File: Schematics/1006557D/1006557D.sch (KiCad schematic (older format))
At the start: 9 parts, among them J1 ConnectorBlockI, X1 OvalBody2, X2 NorBody, X3 ArrowTwiddle, X4 ArrowTwiddle

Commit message: Completed and proofed CAD transcription of drawing 1006557D (Block I AGC module A36 electrical schematic).
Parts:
- added unit 73 of J1
- added unit 70 of J1
- added unit 77 of J1
- added unit 76 of J1
- added unit 75 of J1
- added unit 79 of J1
- added unit 129 of J1
- added unit 74 of J1
- added unit 128 of J1
- added unit 49 of J1
- added unit 45 of J1
- added unit 43 of J1
- added unit 41 of J1
- added unit 62 of J1
- added unit 65 of J1
- added unit 111 of J1
- added unit 113 of J1
- added unit 114 of J1
- added unit 115 of J1
- added unit 116 of J1
- added unit 117 of J1
- added unit 118 of J1
- added unit 50 of J1
- added unit 53 of J1
- added unit 52 of J1
- added unit 54 of J1
- added unit 57 of J1
- added unit 56 of J1
- added unit 36 of J1
- added unit 64 of J1
- added unit 103 of J1
- added unit 101 of J1
- added unit 100 of J1
- added unit 107 of J1
- added unit 106 of J1
- added unit 105 of J1
- added unit 109 of J1
- added unit 108 of J1
- added unit 28 of J1
- added unit 29 of J1
- added unit 25 of J1
- added unit 27 of J1
- added unit 21 of J1
- added unit 16 of J1
- added unit 14 of J1
- added unit 58 of J1
- added unit 137 of J1
- added unit 135 of J1
- added unit 130 of J1
- added unit 131 of J1
- added unit 39 of J1
- added unit 38 of J1
- added unit 102 of J1
- added unit 33 of J1
- added unit 32 of J1
- added unit 20 of J1
- added unit 12 of J1
- added unit 124 of J1
- added unit 122 of J1
- added unit 125 of J1
- added unit 127 of J1
- added unit 126 of J1
- added unit 9 of J1
- added unit 2 of J1
- added unit 90 of J1
- added unit 1 of J1
- added unit 4 of J1
- added unit 139 of J1
- added unit 83 of J1
- added unit 80 of J1
- added unit 81 of J1
- added unit 86 of J1
- added unit 87 of J1
- added unit 84 of J1
- added unit 85 of J1
- added unit 89 of J1
- added unit 15 of J1
- added unit 11 of J1
- added unit 19 of J1
- added unit 18 of J1
- added unit 99 of J1
- added unit 98 of J1
- added unit 94 of J1
- added unit 97 of J1
- added unit 91 of J1
- added unit 82 of J1
- added unit 92 of J1
- added unit 46 of J1
- added unit 63 of J1
- added unit 67 of J1
- added unit 68 of J1
- added unit 69 of J1
- added unit 104 of J1
- added unit 40 of J1
- added unit 142 of J1
- added unit 141 of J1
- added unit 140 of J1
- added unit 42 of J1
- added unit 110 of J1
- added U1, U10, U12, U73, U80, U81, U9: D3NOR-+3VDC-0VDC-block1-1_3-___, symbol D3NOR-+3VDC-0VDC-block1:D3NOR-+3VDC-0VDC-block1-1_3-___
- added U100, U104, U108, U120, U5, U72, U92: D3NOR-+3VDC-0VDC-block1-3_5-___, symbol D3NOR-+3VDC-0VDC-block1:D3NOR-+3VDC-0VDC-block1-3_5-___
- added U101, U107, U119, U13, U18, U21, U22, U26, U37, U41, U42, U45, U46, U52, U53, U57, U69, U70, U78, U82: D3NOR-+3VDC-0VDC-block1-_3_-___, symbol D3NOR-+3VDC-0VDC-block1:D3NOR-+3VDC-0VDC-block1-_3_-___
- added U102, U11, U110, U118, U85, U89, U97: D3NOR-+3VDC-0VDC-block1-13_-___, symbol D3NOR-+3VDC-0VDC-block1:D3NOR-+3VDC-0VDC-block1-13_-___
- added U106, U16, U20, U55, U71, U75, U87, U91, U95, U99: D3NOR-+3VDC-0VDC-block1-153-___, symbol D3NOR-+3VDC-0VDC-block1:D3NOR-+3VDC-0VDC-block1-153-___
- added U109, U113, U117, U17, U29, U30, U38, U50, U54, U61, U62, U90, U93, U94, U98: D3NOR-+3VDC-0VDC-block1-_1_-___, symbol D3NOR-+3VDC-0VDC-block1:D3NOR-+3VDC-0VDC-block1-_1_-___
- added U111, U115, U64: D3NOR-NC-0VDC-expander-block1-_5_-___, symbol D3NOR-NC-0VDC-expander-block1:D3NOR-NC-0VDC-expander-block1-_5_-___
- added U114, U8: D3NOR-+3VDC-0VDC-block1-31_-___, symbol D3NOR-+3VDC-0VDC-block1:D3NOR-+3VDC-0VDC-block1-31_-___
- added U14: D3NOR-NC-0VDC-expander-block1-1_3-___, symbol D3NOR-NC-0VDC-expander-block1:D3NOR-NC-0VDC-expander-block1-1_3-___
- added U15, U19, U23, U27, U28, U3, U31, U35, U39, U47, U51, U59, U63, U7, U79, U83: D3NOR-+3VDC-0VDC-block1-135-___, symbol D3NOR-+3VDC-0VDC-block1:D3NOR-+3VDC-0VDC-block1-135-___
- added U24, U32, U36, U4, U40, U43, U44, U48, U84, U88, U96: D3NOR-+3VDC-0VDC-block1-315-___, symbol D3NOR-+3VDC-0VDC-block1:D3NOR-+3VDC-0VDC-block1-315-___
- added U25, U33, U34, U65, U67, U86: D3NOR-+3VDC-0VDC-block1-_5_-___, symbol D3NOR-+3VDC-0VDC-block1:D3NOR-+3VDC-0VDC-block1-_5_-___
- added U6, U60, U68, U76: D3NOR-+3VDC-0VDC-block1-1_5-___, symbol D3NOR-+3VDC-0VDC-block1:D3NOR-+3VDC-0VDC-block1-1_5-___
- added X10, X5, X6, X7, X8, X9: Node2, symbol AGC_DSKY:Node2
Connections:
- net +3VDC: now also U1.8 (+3VDC), U10.8 (+3VDC), U100.8 (+3VDC), U101.8 (+3VDC), U102.8 (+3VDC), U104.8 (+3VDC), U106.8 (+3VDC), U107.8 (+3VDC), U108.8 (+3VDC), U109.8 (+3VDC), U11.8 (+3VDC), U110.8 (+3VDC), U113.8 (+3VDC), U114.8 (+3VDC), U117.8 (+3VDC), U118.8 (+3VDC), U119.8 (+3VDC), U12.8 (+3VDC), U120.8 (+3VDC), U13.8 (+3VDC), U15.8 (+3VDC), U16.8 (+3VDC), U17.8 (+3VDC), U18.8 (+3VDC), U19.8 (+3VDC), U20.8 (+3VDC), U21.8 (+3VDC), U22.8 (+3VDC), U23.8 (+3VDC), U24.8 (+3VDC), U25.8 (+3VDC), U26.8 (+3VDC), U27.8 (+3VDC), U28.8 (+3VDC), U29.8 (+3VDC), U3.8 (+3VDC), U30.8 (+3VDC), U31.8 (+3VDC), U32.8 (+3VDC), U33.8 (+3VDC), U34.8 (+3VDC), U35.8 (+3VDC), U36.8 (+3VDC), U37.8 (+3VDC), U38.8 (+3VDC), U39.8 (+3VDC), U4.8 (+3VDC), U40.8 (+3VDC), U41.8 (+3VDC), U42.8 (+3VDC), U43.8 (+3VDC), U44.8 (+3VDC), U45.8 (+3VDC), U46.8 (+3VDC), U47.8 (+3VDC), U48.8 (+3VDC), U5.8 (+3VDC), U50.8 (+3VDC), U51.8 (+3VDC), U52.8 (+3VDC), U53.8 (+3VDC), U54.8 (+3VDC), U55.8 (+3VDC), U57.8 (+3VDC), U59.8 (+3VDC), U6.8 (+3VDC), U60.8 (+3VDC), U61.8 (+3VDC), U62.8 (+3VDC), U63.8 (+3VDC), U65.8 (+3VDC), U67.8 (+3VDC), U68.8 (+3VDC), U69.8 (+3VDC), U7.8 (+3VDC), U70.8 (+3VDC), U71.8 (+3VDC), U72.8 (+3VDC), U73.8 (+3VDC), U75.8 (+3VDC), U76.8 (+3VDC), U78.8 (+3VDC), U79.8 (+3VDC), U8.8 (+3VDC), U80.8 (+3VDC), U81.8 (+3VDC), U82.8 (+3VDC), U83.8 (+3VDC), U84.8 (+3VDC), U85.8 (+3VDC), U86.8 (+3VDC), U87.8 (+3VDC), U88.8 (+3VDC), U89.8 (+3VDC), U9.8 (+3VDC), U90.8 (+3VDC), U91.8 (+3VDC), U92.8 (+3VDC), U93.8 (+3VDC), U94.8 (+3VDC), U95.8 (+3VDC), U96.8 (+3VDC), U97.8 (+3VDC), U98.8 (+3VDC), U99.8 (+3VDC)
- net 0VDC: now also U1.4 (0VDC), U1.5 (0VDC), U10.4 (0VDC), U10.5 (0VDC), U100.1 (0VDC), U100.4 (0VDC), U101.1 (0VDC), U101.4 (0VDC), U101.5 (0VDC), U102.4 (0VDC), U102.5 (0VDC), U104.1 (0VDC), U104.4 (0VDC), U106.4 (0VDC), U107.1 (0VDC), U107.4 (0VDC), U107.5 (0VDC), U108.1 (0VDC), U108.4 (0VDC), U109.3 (0VDC), U109.4 (0VDC), U109.5 (0VDC), U11.4 (0VDC), U11.5 (0VDC), U110.4 (0VDC), U110.5 (0VDC), U111.1 (0VDC), U111.3 (0VDC), U111.4 (0VDC), U113.3 (0VDC), U113.4 (0VDC), U113.5 (0VDC), U114.4 (0VDC), U114.5 (0VDC), U115.1 (0VDC), U115.3 (0VDC), U115.4 (0VDC), U117.3 (0VDC), U117.4 (0VDC), U117.5 (0VDC), U118.4 (0VDC), U118.5 (0VDC), U119.1 (0VDC), U119.4 (0VDC), U119.5 (0VDC), U12.4 (0VDC), U12.5 (0VDC), U120.1 (0VDC), U120.4 (0VDC), U13.1 (0VDC), U13.4 (0VDC), U13.5 (0VDC), U14.4 (0VDC), U14.5 (0VDC), U15.4 (0VDC), U16.4 (0VDC), U17.3 (0VDC), U17.4 (0VDC), U17.5 (0VDC), U18.1 (0VDC), U18.4 (0VDC), U18.5 (0VDC), U19.4 (0VDC), U20.4 (0VDC), U21.1 (0VDC), U21.4 (0VDC), U21.5 (0VDC), U22.1 (0VDC), U22.4 (0VDC), U22.5 (0VDC), U23.4 (0VDC), U24.4 (0VDC), U25.1 (0VDC), U25.3 (0VDC), U25.4 (0VDC), U26.1 (0VDC), U26.4 (0VDC), U26.5 (0VDC), U27.4 (0VDC), U28.4 (0VDC), U29.3 (0VDC), U29.4 (0VDC), U29.5 (0VDC), U3.4 (0VDC), U30.3 (0VDC), U30.4 (0VDC), U30.5 (0VDC), U31.4 (0VDC), U32.4 (0VDC), U33.1 (0VDC), U33.3 (0VDC), U33.4 (0VDC), U34.1 (0VDC), U34.3 (0VDC), U34.4 (0VDC), U35.4 (0VDC), U36.4 (0VDC), U37.1 (0VDC), U37.4 (0VDC), U37.5 (0VDC), U38.3 (0VDC), U38.4 (0VDC), U38.5 (0VDC), U39.4 (0VDC), U4.4 (0VDC), U40.4 (0VDC), U41.1 (0VDC), U41.4 (0VDC), U41.5 (0VDC), U42.1 (0VDC), U42.4 (0VDC), U42.5 (0VDC), U43.4 (0VDC), U44.4 (0VDC), U45.1 (0VDC), U45.4 (0VDC), U45.5 (0VDC), U46.1 (0VDC), U46.4 (0VDC), U46.5 (0VDC), U47.4 (0VDC), U48.4 (0VDC), U5.1 (0VDC), U5.4 (0VDC), U50.3 (0VDC), U50.4 (0VDC), U50.5 (0VDC), U51.4 (0VDC), U52.1 (0VDC), U52.4 (0VDC), U52.5 (0VDC), U53.1 (0VDC), U53.4 (0VDC), U53.5 (0VDC), U54.3 (0VDC), U54.4 (0VDC), U54.5 (0VDC), U55.4 (0VDC), U57.1 (0VDC), U57.4 (0VDC), U57.5 (0VDC), U59.4 (0VDC), U6.3 (0VDC), U6.4 (0VDC), U60.3 (0VDC), U60.4 (0VDC), U61.3 (0VDC), U61.4 (0VDC), U61.5 (0VDC), U62.3 (0VDC), U62.4 (0VDC), U62.5 (0VDC), U63.4 (0VDC), U64.1 (0VDC), U64.3 (0VDC), U64.4 (0VDC), U65.1 (0VDC), U65.3 (0VDC), U65.4 (0VDC), U67.1 (0VDC), U67.3 (0VDC), U67.4 (0VDC), U68.3 (0VDC), U68.4 (0VDC), U69.1 (0VDC), U69.4 (0VDC), U69.5 (0VDC), U7.4 (0VDC), U70.1 (0VDC), U70.4 (0VDC), U70.5 (0VDC), U71.4 (0VDC), U72.1 (0VDC), U72.4 (0VDC), U73.4 (0VDC), U73.5 (0VDC), U75.4 (0VDC), U76.3 (0VDC), U76.4 (0VDC), U78.1 (0VDC), U78.4 (0VDC), U78.5 (0VDC), U79.4 (0VDC), U8.4 (0VDC), U8.5 (0VDC), U80.4 (0VDC), U80.5 (0VDC), U81.4 (0VDC), U81.5 (0VDC), U82.1 (0VDC), U82.4 (0VDC), U82.5 (0VDC), U83.4 (0VDC), U84.4 (0VDC), U85.4 (0VDC), U85.5 (0VDC), U86.1 (0VDC), U86.3 (0VDC), U86.4 (0VDC), U87.4 (0VDC), U88.4 (0VDC), U89.4 (0VDC), U89.5 (0VDC), U9.4 (0VDC), U9.5 (0VDC), U90.3 (0VDC), U90.4 (0VDC), U90.5 (0VDC), U91.4 (0VDC), U92.1 (0VDC), U92.4 (0VDC), U93.3 (0VDC), U93.4 (0VDC), U93.5 (0VDC), U94.3 (0VDC), U94.4 (0VDC), U94.5 (0VDC), U95.4 (0VDC), U96.4 (0VDC), U97.4 (0VDC), U97.5 (0VDC), U98.3 (0VDC), U98.4 (0VDC), U98.5 (0VDC), U99.4 (0VDC)
- new net: J1.73, U63.7
- new net: J1.70, U62.7
- new net: J1.77, U67.7, U75.1
- new net: J1.76, U64.7
- new net: J1.75, U67.5
- new net: U19.1, U3.1, U31.1, U37.7, U41.7, U43.3, U51.1, U59.1
- new net: U19.3, U25.7, U27.3, U51.3, U55.3
- new net: U13.7, U15.5, U17.7, U19.5, U27.5, U3.5, U31.5, U35.5
- new net: J1.19, U19.7
- new net: U10.3, U12.7, U16.1, U20.1
- new net: J1.16, U16.3
- new net: J1.28, U16.5, U20.5
- new net: J1.18, U16.7, U22.3
- new net: J1.15, U1.1, U13.3, U17.1, U7.1
- new net: J1.79, U55.7
- new net: U15.1, U21.7, U27.1, U29.7, U35.1, U47.1, U55.1, U63.1
- new net: U15.3, U3.3, U43.1, U47.3, U65.7
- new net: J1.11, U15.7
- new net: U12.1, U8.7
- new net: U10.7, U12.3
- new net: U10.1, U14.7, U6.7
- new net: U11.1, U7.7
- new net: U11.3, U23.1, U39.3, U9.7
- new net: U11.7, U9.3
- new net: U114.7, U118.1, U84.1, U88.1, U96.1
- new net: J1.108, U94.1, U96.3
- new net: J1.130, U100.5, U104.3, U108.5, U120.5, U60.5, U68.5, U76.5, U84.5, U88.5, U92.5, U96.5
- new net: J1.114, U96.7
- new net: U85.7, U89.3, U97.3
- new net: J1.117, U101.3, U93.1, U97.7
- new net: U106.5, U94.7
- new net: U101.7, U71.1, U79.1, U87.1, U91.1, U93.7, U95.1, U99.1
- new net: J1.113, U95.3, U99.3
- new net: J1.83, U71.5, U87.5, U95.5
- new net: J1.111, U95.7
- new net: J1.106, U92.3
- new net: J1.110, U92.7
- new net: U106.7, U110.3, U90.1
- new net: U102.3, U90.7
- new net: J1.109, U87.3, U91.3
- new net: J1.107, U79.3, U91.5, U99.5
- new net: J1.105, U91.7
- new net: J1.40, U34.5
- new net: U24.3, U28.1, U32.3, U34.7
- new net: J1.115, U99.7
- new net: J1.129, U111.7
- new net: J1.20, U18.3
- new net: U18.7, U24.1, U36.1, U40.1
- new net: J1.74, U64.5
- new net: J1.128, U108.7
- new net: U5.7, U9.1
- new net: U4.7, U8.1
- new net: U102.7, U118.3
- new net: U114.3, U118.7
- new net: J1.49, U43.7
- new net: J1.63, U1.3, U45.3, U53.3, U7.3
- new net: U1.7, U5.3
- new net: J1.1, U3.7
- new net: J1.45, U39.5
- new net: J1.97, U5.5, U7.5, U81.3, U83.5
- new net: J1.43, U37.3, U39.7, U41.3
- new net: J1.41, U33.5
- new net: U73.7, U81.1
- new net: U81.7, U85.1
- new net: U60.1, U68.1, U70.7, U76.1, U80.1
- new net: J1.86, U80.7
- new net: J1.103, U73.3, U83.1
- new net: J1.99, U73.1, U83.3
- new net: U83.7, U89.1
- new net: J1.94, U78.3, U82.3
- new net: U85.3, U89.7
- new net: J1.98, U84.3, U86.5
- new net: J1.100, U84.7
- new net: J1.101, U87.7
- new net: U106.1, U86.7
- new net: J1.102, U88.3, U98.1
- new net: J1.104, U88.7
- new net: J1.116, U100.3
- new net: J1.118, U100.7
- new net: J1.62, U52.7
- new net: J1.65, U57.7
- new net: J1.50, U42.7
- new net: J1.53, U47.7
- new net: J1.52, U44.7
- new net: J1.54, U48.7
- new net: J1.57, U51.7
- new net: J1.56, U46.3, U50.1
- new net: J1.12, U20.7, U30.1
- new net: J1.85, U71.3, U79.5
- new net: J1.91, U79.7
- new net: J1.36, U28.7
- new net: J1.89, U75.3
- new net: J1.87, U75.5
- new net: U61.1, U69.3, U75.7
- new net: J1.90, U76.7
- new net: U70.3, U72.7
- new net: J1.81, U71.7
- new net: J1.82, U72.3
- new net: J1.84, U72.5
- new net: U106.3, U98.7
- new net: U22.7, U24.5, U32.5, U40.5, U48.5
- new net: J1.14, U24.7
- new net: J1.64, U54.7
- new net: J1.127, U107.3
- new net: J1.125, U107.7
- new net: J1.126, U108.3
- new net: J1.141, U109.1, U113.1, U117.1, U119.3
- new net: J1.137, U109.7, U117.7
- new net: U110.7, U114.1
- new net: J1.29, U25.5
- new net: J1.80, U68.7
- new net: J1.25, U23.5
- new net: J1.69, U65.5
- new net: U31.3, U33.7, U35.3, U59.3, U63.3
- new net: U43.5, U45.7, U47.5, U51.5, U53.7, U55.5, U59.5, U63.5
- new net: J1.21, U21.3, U23.7, U29.1
- new net: J1.68, U60.7
- new net: J1.122, U104.5
- new net: J1.124, U104.7
- new net: J1.139, U113.7, U119.7
- new net: U28.5, U30.7, U36.5, U44.5
- new net: J1.131, U111.5, U115.5
- new net: J1.135, U115.7
- new net: J1.58, U42.3, U46.7, U50.7, U52.3, U54.1, U62.1
- new net: J1.67, U59.7
- new net: J1.39, U35.7
- new net: J1.38, U32.7
- new net: J1.33, U31.7
- new net: J1.140, U120.3
- new net: J1.142, U120.7
- new net: U26.7, U28.3, U32.1, U44.1, U48.1
- new net: U36.3, U38.7, U40.3, U44.3, U48.3
- new net: J1.46, U40.7
- new net: J1.9, U27.7
- new net: J1.42, U36.7
- new net RATE_: J1.27, U23.3, U39.1, U57.3, U61.7, U69.7, U97.1, X10.1
- new net SB0_: J1.92, U102.1, U110.1, U6.1, U78.7, U8.3, U80.3, U82.7, X8.1, X9.1
- new net W2TD01: J1.2, U14.3, U20.3, U4.5, X5.1
- new net W2TD02: J1.32, U14.1, U26.3, U4.1, X6.1
- new net W2TD03: J1.4, U38.1, U4.3, U6.5, X7.1
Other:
- note added: "//"
- note added: "2M5\n77090"
- note added: "___"
- note added: "____________"
- note added: "{"
- note removed: "2M5\n33090"
- moved on the sheet: C1, C2, C3, C4

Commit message: Apparently, in the first Block I AGC drawing I transcribed to CAD, I misread the AGC4 connector pin name associated with AGC5 connector pin 120 as "69" when it was really "89".  This error had propagated to all of the Block I drawings except the most recent (1006550F) and the transcriptions I had made from ND-1021041 rather than from drawings.
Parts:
- J1: agc4 069 -> 089
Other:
- note added: "C"
- note added: "D"
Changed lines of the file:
@@
 F 2 "" H 37450 27625 140 0001 C CNN
 F 3 "" H 37450 27625 140 0001 C CNN
-F 4 "069" H 37450 27300 100 0000 C TNB "agc4"
+F 4 "089" H 37450 27300 100 0000 C TNB "agc4"
 F 5 "0VDC" H 37450 27375 140 0001 C BNB "Caption"
 	120  37450 27150
@@
 	37968 1965 43503 1965
 Text Notes 38153 1935 0    140  ~ 28
-B
+D
 Text Notes 38533 1925 0    140  ~ 28
 REVISED PER TDRR 06035
@@
 REVISED PER TDRR 04523
 Text Notes 38150 1675 0    140  ~ 28
-A
+C
 Text Notes 35225 5200 0    140  ~ 28
 Notes from the Virtual AGC Project:\n1. This CAD drawing was transcribed from the original Apollo Program \n   drawing 1006557D. — RSB 2019\n2. The original drawing did not show reference designators or pin numbers \n   for the NOR gates, so this CAD drawing does not show them either.  \n   However, those items were derived instead from the original Apollo \n   signal wiring diagram, 1006137-, and can be accessed by editing the \n   NOR gates within a CAD system. — RSB 2019\n3. The numbered oval pads comprise connector J1. — RSB 2019\n4. Wiring diagram 1006137- indicates that the inputs of gate 77103 are \n   SB0/  and W2TD01, whereas schematic 1006557D (as well as revs "-" \n   through "C") indicate SB0/ and W2TD03.  I interpret this as an error in\n   rev "-" of the wiring diagram. — RSB 2019

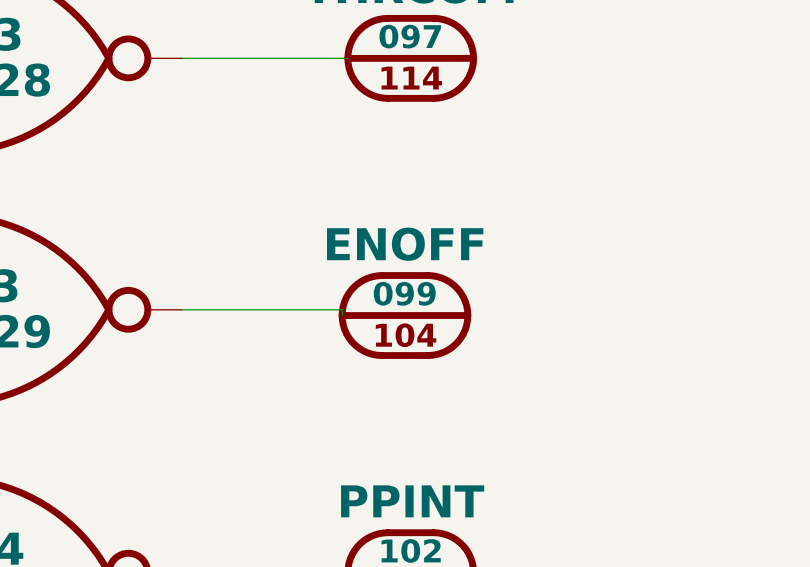
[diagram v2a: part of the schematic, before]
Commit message: Made visual fixes with eelint.  ERC passes (if current bugs in KiCad ERC are worked around).  Netlist unchanged.
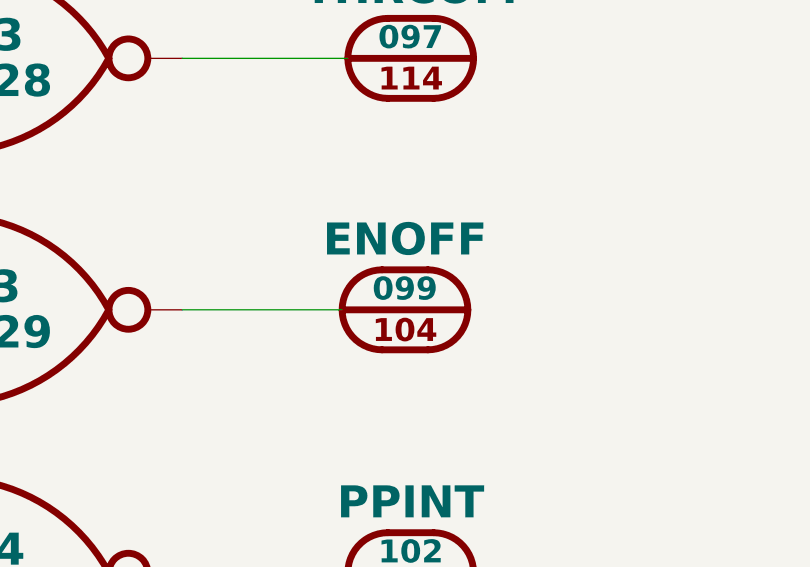
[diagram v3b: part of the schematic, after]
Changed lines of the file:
@@
-EESchema Schematic File Version 4
-LIBS:module-cache
+EESchema Schematic File Version 5
+LIBS:errors-cache
 EELAYER 29 0
 EELAYER END
 $Descr E 44000 34000
 encoding utf-8
-Sheet 2 2
+Sheet 1 1
 Title ""
 Date ""
@@
 L AGC_DSKY:ConnectorBlockI J1
 U 104 1 5C532C8E
-P 33725 13600
-F 0 "J1" H 33725 13925 140 0001 C CNN
-F 1 "ConnectorBlockI" H 33725 14025 140 0001 C CNN
-F 2 "" H 33725 14075 140 0001 C CNN
-F 3 "" H 33725 14075 140 0001 C CNN
-F 4 "099" H 33725 13750 100 0000 C TNB "agc4"
-F 5 "ENOFF" H 33725 13825 140 0000 C BNB "Caption"
-F 6 "" H 33725 13375 140 0000 C TNB "Caption2"
-	104  33725 13600
+P 33725 13575
+F 0 "J1" H 33725 13900 140 0001 C CNN
+F 1 "ConnectorBlockI" H 33725 14000 140 0001 C CNN
+F 2 "" H 33725 14050 140 0001 C CNN
+F 3 "" H 33725 14050 140 0001 C CNN
+F 4 "099" H 33725 13725 100 0000 C TNB "agc4"
+F 5 "ENOFF" H 33725 13800 140 0000 C BNB "Caption"
+F 6 "" H 33725 13350 140 0000 C TNB "Caption2"
+	104  33725 13575
 	-1   0    0    -1
 $EndComp
@@
 	32750 13575 33450 13575
 Wire Wire Line
-	33450 13575 33450 13600
-Wire Wire Line
 	30950 12750 30450 12750
